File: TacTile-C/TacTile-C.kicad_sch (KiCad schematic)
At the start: 42 parts, among them J1 Conn_01x02, J10 Conn_01x02, J11 Conn_01x02, J12 Conn_01x02, J13 Conn_01x02, J14 Conn_01x02, J15 Conn_01x02, J16 Conn_01x02, J17 Conn_01x02, J2 Conn_01x02, J3 Conn_01x02, J4 Conn_01x02, J5 Conn_01x02, J6 Conn_01x02, J7 Conn_01x02, J8 Conn_01x02, J9 Conn_01x02, U1 74HC4051, U10 74LVC1G18, U2 74HC4051, U3 74HC4051, U4 74HC4051, U5 74HC4051, U7 74LVC1G18, U8 74HC4051, U9 74HC4051

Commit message: Began layout and routing of board C
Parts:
- added J18: Conn_01x04, Connector_PinHeader_1.27mm:PinHeader_1x04_P1.27mm_Vertical, symbol Connector_Generic:Conn_01x04
- added J19: Conn_01x05, Connector_PinHeader_1.27mm:PinHeader_1x05_P1.27mm_Vertical, symbol Connector_Generic:Conn_01x05
- added J20, J21: Conn_01x02, Connector_PinHeader_1.27mm:PinHeader_1x02_P1.27mm_Vertical, symbol Connector_Generic:Conn_01x02
- renumbered J2 to J1, J11 to J10, J12 to J11, J13 to J12, J14 to J13, J15 to J14, J16 to J15, J17 to J16, J1 to J17, J3 to J2, J4 to J3, J5 to J4, J6 to J5, J7 to J6, J8 to J7, J9 to J8, J10 to J9, U7 to U1, U10 to U1, U1 to U2, U2 to U3, U3 to U4, U4 to U5, U5 to U6, U8 to U7, U9 to U8
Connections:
- net GND: now also J20.2 (Pin_2)
- net LEN: now also J21.2 (Pin_2)
- net LS0: now also J18.1 (Pin_1)
- net LS1: now also J18.2 (Pin_2)
- net LS2: now also J18.3 (Pin_3)
- net LS3: now also J18.4 (Pin_4)
- net LS4: now also J19.1 (Pin_1)
- net LS5: now also J19.2 (Pin_2)
- net LS6: now also J19.3 (Pin_3)
- net LS7: now also J19.4 (Pin_4)
- net LS8: now also J19.5 (Pin_5)
- net VCC: now also J21.1 (Pin_1)
- net VIN: now also J20.1 (Pin_1)
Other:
- moved on the sheet: J17

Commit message: Mounted ICs without sockets to save space
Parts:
- U1: footprint Package_DIP:DIP-6_W7.62mm_Socket -> Package_DIP:DIP-6_W7.62mm
- U2, U3, U4, U5, U6, U7, U8: footprint Package_DIP:DIP-16_W7.62mm_Socket -> Package_DIP:DIP-16_W7.62mm
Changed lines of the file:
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@@
       (effects (font (size 1.27 1.27)) (justify left))
     )
-    (property "Footprint" "Package_DIP:DIP-16_W7.62mm_Socket" (at 149.86 105.41 0)
+    (property "Footprint" "Package_DIP:DIP-16_W7.62mm" (at 149.86 105.41 0)
       (effects (font (size 1.27 1.27)) hide)
     )
@@
       (effects (font (size 1.27 1.27)) (justify left))
     )
-    (property "Footprint" "Package_DIP:DIP-16_W7.62mm_Socket" (at 135.89 144.78 0)
+    (property "Footprint" "Package_DIP:DIP-16_W7.62mm" (at 135.89 144.78 0)
       (effects (font (size 1.27 1.27)) hide)
     )
@@
       (effects (font (size 1.27 1.27)) (justify left))
     )
-    (property "Footprint" "Package_DIP:DIP-16_W7.62mm_Socket" (at 151.13 227.33 0)
+    (property "Footprint" "Package_DIP:DIP-16_W7.62mm" (at 151.13 227.33 0)
       (effects (font (size 1.27 1.27)) hide)
     )
@@
       (effects (font (size 1.27 1.27)))
     )
-    (property "Footprint" "Package_DIP:DIP-6_W7.62mm_Socket" (at 133.35 172.72 0)
+    (property "Footprint" "Package_DIP:DIP-6_W7.62mm" (at 133.35 172.72 0)
       (effects (font (size 1.27 1.27)) hide)
     )
@@
       (effects (font (size 1.27 1.27)) (justify left))
     )
-    (property "Footprint" "Package_DIP:DIP-16_W7.62mm_Socket" (at 120.65 105.41 0)
+    (property "Footprint" "Package_DIP:DIP-16_W7.62mm" (at 120.65 105.41 0)
       (effects (font (size 1.27 1.27)) hide)
     )
@@
       (effects (font (size 1.27 1.27)) (justify left))
     )
-    (property "Footprint" "Package_DIP:DIP-16_W7.62mm_Socket" (at 120.65 227.33 0)
+    (property "Footprint" "Package_DIP:DIP-16_W7.62mm" (at 120.65 227.33 0)
       (effects (font (size 1.27 1.27)) hide)
     )
@@
       (effects (font (size 1.27 1.27)) (justify left))
     )
-    (property "Footprint" "Package_DIP:DIP-16_W7.62mm_Socket" (at 91.44 105.41 0)
+    (property "Footprint" "Package_DIP:DIP-16_W7.62mm" (at 91.44 105.41 0)
       (effects (font (size 1.27 1.27)) hide)
     )
@@
       (effects (font (size 1.27 1.27)) (justify left))
     )
-    (property "Footprint" "Package_DIP:DIP-16_W7.62mm_Socket" (at 179.07 105.41 0)
+    (property "Footprint" "Package_DIP:DIP-16_W7.62mm" (at 179.07 105.41 0)
       (effects (font (size 1.27 1.27)) hide)
     )
@@
       (effects (font (size 1.27 1.27)) (justify left))
     )
-    (property "Footprint" "Package_DIP:DIP-6_W7.62mm_Socket" (at 177.8 26.67 0)
-      (effects (font (size 1.27 1.27)) hide)
-    )
+    (property "Footprint" "Package_DIP:DIP-6_W7.62mm" (at 177.8 26.67 0)
+      (effects (font (size 1.27 1.27)) hide)
+    )

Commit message: Enlarged B-C interface to 2.54 pitch connectors
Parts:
- J18: footprint Connector_PinHeader_1.27mm:PinHeader_1x04_P1.27mm_Vertical -> Connector_PinHeader_2.54mm:PinHeader_1x04_P2.54mm_Vertical
- J19: footprint Connector_PinHeader_1.27mm:PinHeader_1x05_P1.27mm_Vertical -> Connector_PinHeader_2.54mm:PinHeader_1x05_P2.54mm_Vertical
- J20, J21: footprint Connector_PinHeader_1.27mm:PinHeader_1x02_P1.27mm_Vertical -> Connector_PinHeader_2.54mm:PinHeader_1x02_P2.54mm_Vertical
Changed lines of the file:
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@@
       (effects (font (size 1.27 1.27)) (justify left))
     )
-    (property "Footprint" "Connector_PinHeader_1.27mm:PinHeader_1x05_P1.27mm_Vertical" (at 27.94 132.08 0)
+    (property "Footprint" "Connector_PinHeader_2.54mm:PinHeader_1x05_P2.54mm_Vertical" (at 27.94 132.08 0)
       (effects (font (size 1.27 1.27)) hide)
     )
@@
       (effects (font (size 1.27 1.27)) (justify left))
     )
-    (property "Footprint" "Connector_PinHeader_1.27mm:PinHeader_1x02_P1.27mm_Vertical" (at 27.94 147.32 0)
+    (property "Footprint" "Connector_PinHeader_2.54mm:PinHeader_1x02_P2.54mm_Vertical" (at 27.94 147.32 0)
       (effects (font (size 1.27 1.27)) hide)
     )
@@
       (effects (font (size 1.27 1.27)) (justify left))
     )
-    (property "Footprint" "Connector_PinHeader_1.27mm:PinHeader_1x02_P1.27mm_Vertical" (at 27.94 162.56 0)
+    (property "Footprint" "Connector_PinHeader_2.54mm:PinHeader_1x02_P2.54mm_Vertical" (at 27.94 162.56 0)
       (effects (font (size 1.27 1.27)) hide)
     )
@@
       (effects (font (size 1.27 1.27)) (justify left))
     )
-    (property "Footprint" "Connector_PinHeader_1.27mm:PinHeader_1x04_P1.27mm_Vertical" (at 27.94 115.57 0)
-      (effects (font (size 1.27 1.27)) hide)
-    )
+    (property "Footprint" "Connector_PinHeader_2.54mm:PinHeader_1x04_P2.54mm_Vertical" (at 27.94 115.57 0)
+      (effects (font (size 1.27 1.27)) hide)
+    )

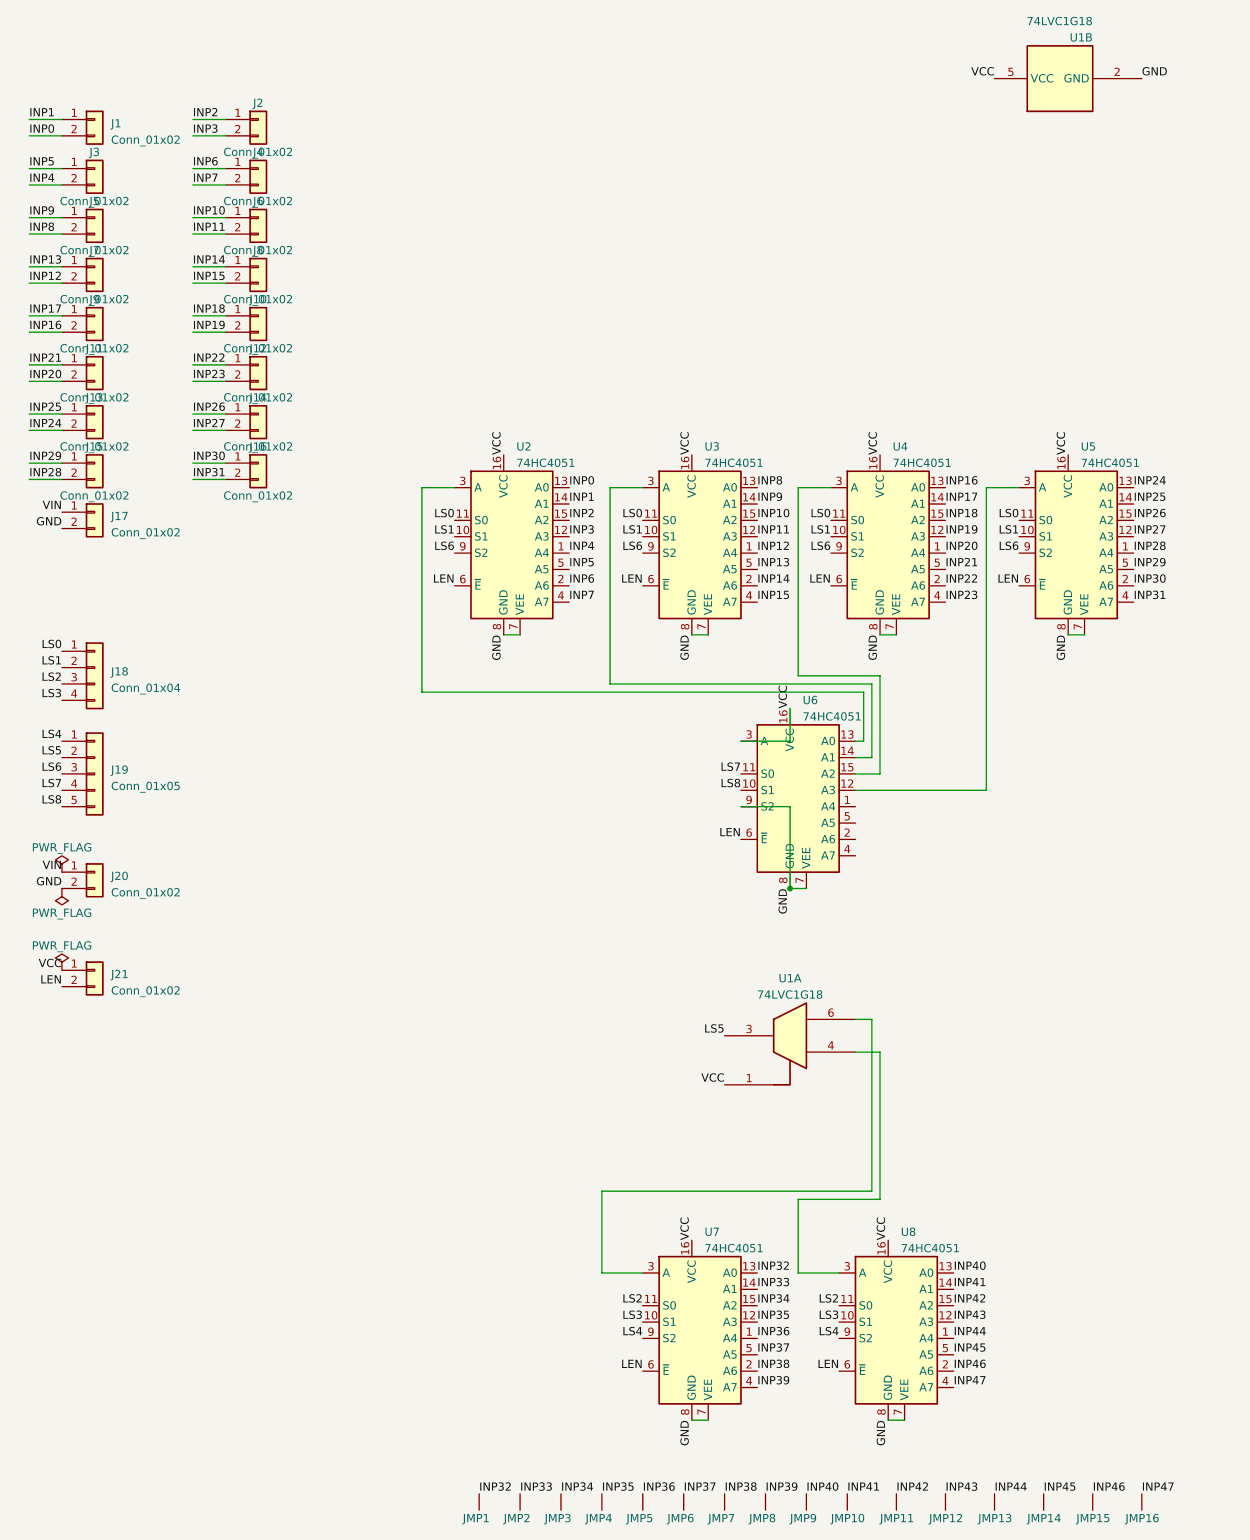
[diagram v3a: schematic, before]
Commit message: Used 16DIP demultiplexer instead of single demultiplexer
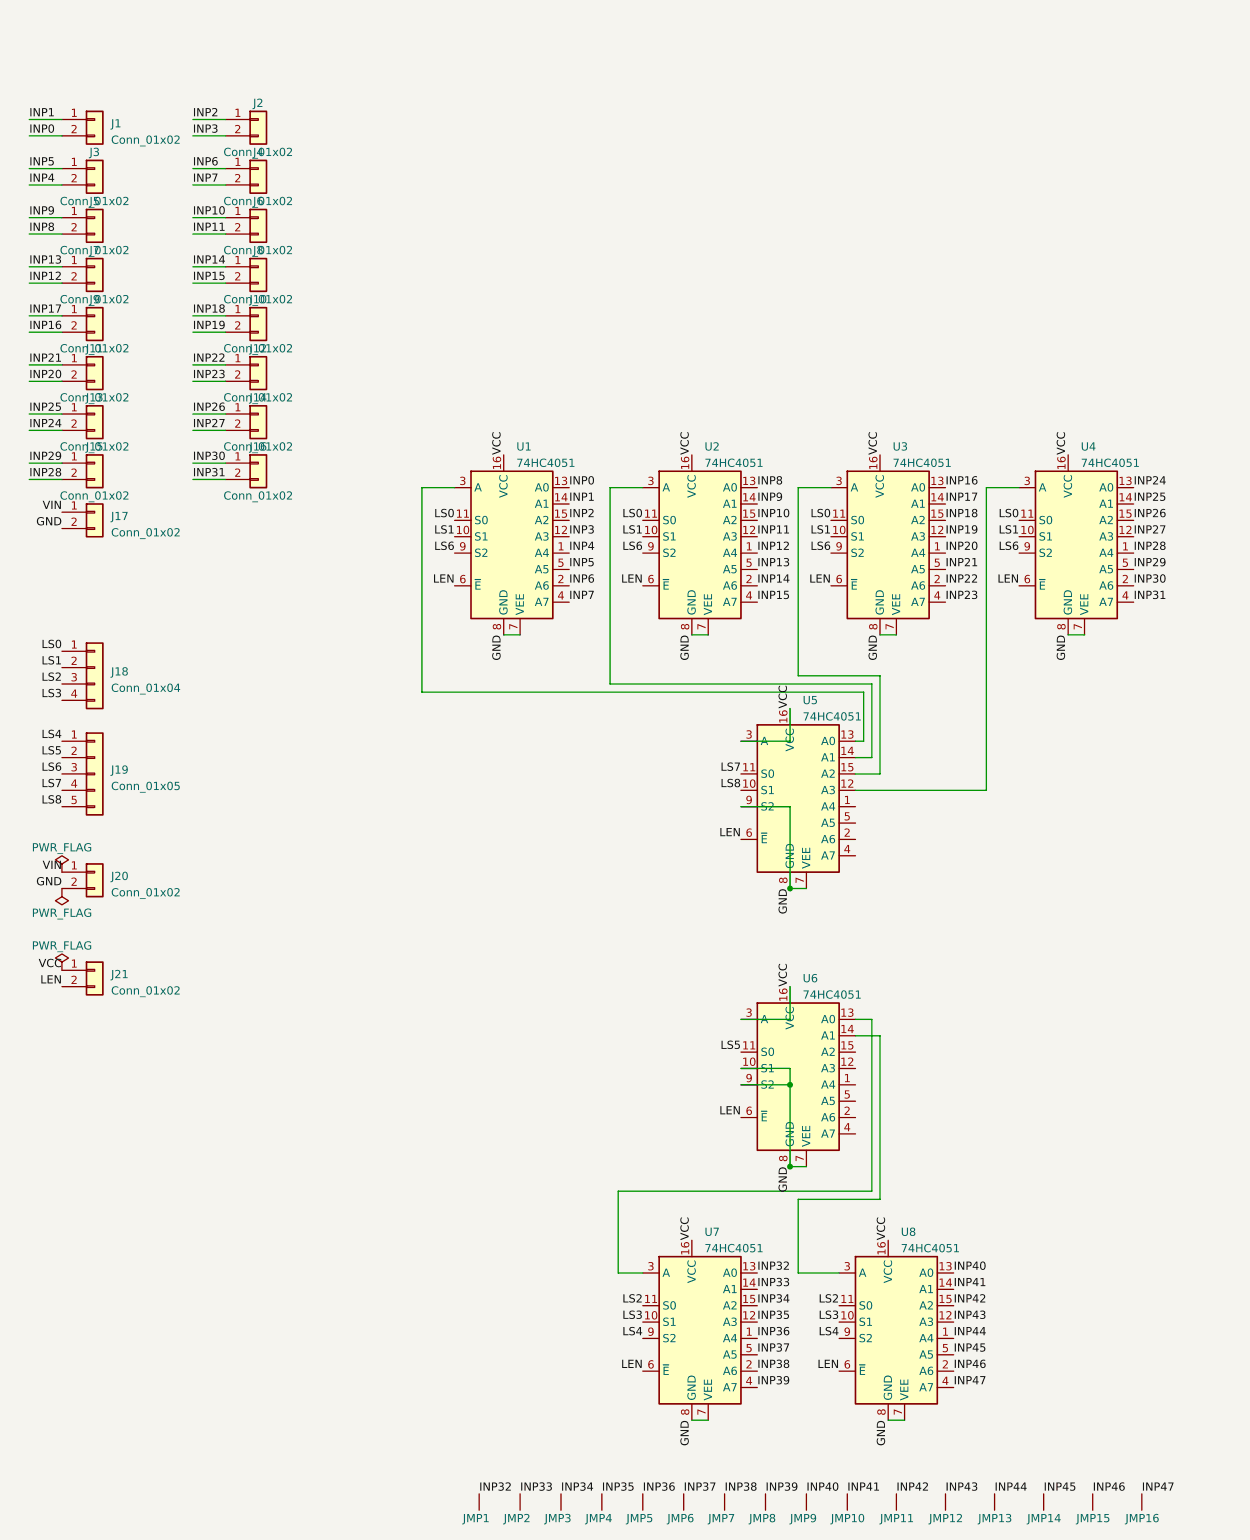
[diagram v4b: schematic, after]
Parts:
- removed U1: 74LVC1G18, Package_DIP:DIP-6_W7.62mm, symbol 74xGxx:74LVC1G18
- added U6: 74HC4051, Package_DIP:DIP-16_W7.62mm, symbol 74xx:74HC4051
- renumbered U2 to U1, U3 to U2, U4 to U3, U5 to U4, U6 to U5
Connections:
- net GND: now also U6.10 (S1), U6.7 (VEE), U6.8 (GND), U6.9 (S2)
- net LEN: now also U6.6 (~{E})
- net LS5: now also U6.11 (S0)
- net VCC: now also U6.16 (VCC), U6.3 (A)
- net at U8.3 (A): now also U6.14 (A1)
- net at U7.3 (A): now also U6.13 (A0)

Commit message: Redid A board with MOSFETs sinking current
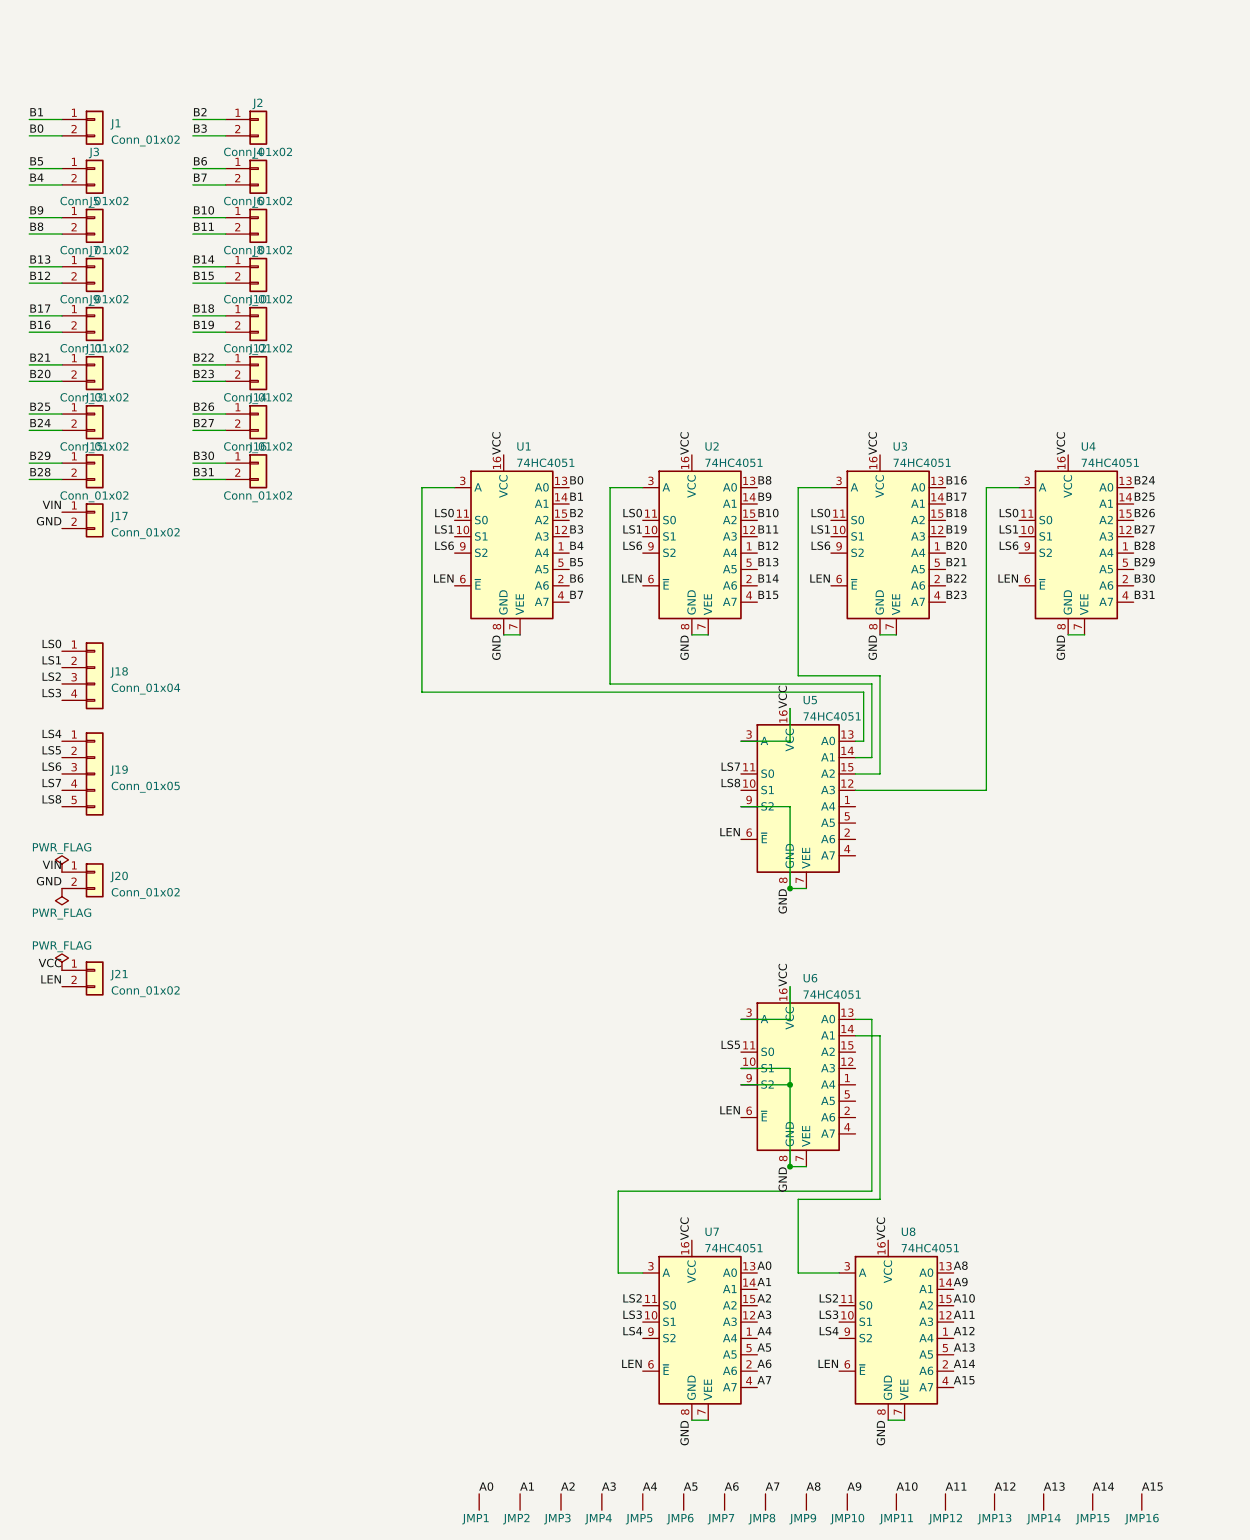
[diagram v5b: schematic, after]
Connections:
- net INP0 renamed B0
- net INP1 renamed B1
- net INP10 renamed B10
- net INP11 renamed B11
- net INP12 renamed B12
- net INP13 renamed B13
- net INP14 renamed B14
- net INP15 renamed B15
- net INP16 renamed B16
- net INP17 renamed B17
- net INP18 renamed B18
- net INP19 renamed B19
- net INP2 renamed B2
- net INP20 renamed B20
- net INP21 renamed B21
- net INP22 renamed B22
- net INP23 renamed B23
- net INP24 renamed B24
- net INP25 renamed B25
- net INP26 renamed B26
- net INP27 renamed B27
- net INP28 renamed B28
- net INP29 renamed B29
- net INP3 renamed B3
- net INP30 renamed B30
- net INP31 renamed B31
- net INP32 renamed A0
- net INP33 renamed A1
- net INP34 renamed A2
- net INP35 renamed A3
- net INP36 renamed A4
- net INP37 renamed A5
- net INP38 renamed A6
- net INP39 renamed A7
- net INP4 renamed B4
- net INP40 renamed A8
- net INP41 renamed A9
- net INP42 renamed A10
- net INP43 renamed A11
- net INP44 renamed A12
- net INP45 renamed A13
- net INP46 renamed A14
- net INP47 renamed A15
- net INP5 renamed B5
- net INP6 renamed B6
- net INP7 renamed B7
- net INP8 renamed B8
- net INP9 renamed B9

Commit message: Added voltage input to A MOSFETs
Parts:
- added JMP17: ~, TacTile:Jumper_Connect, symbol TacTile:Jumper_Connect
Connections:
- net VCC: now also JMP17.1 (A)
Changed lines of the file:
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@@
+    (effects (font (size 1.27 1.27)) (justify left bottom))
+  )
+  (label "VCC" (at 196.85 243.84 0) (fields_autoplaced)
     (effects (font (size 1.27 1.27)) (justify left bottom))
   )
@@
         )
       )
+    )
+  )
+  (symbol (lib_id "TacTile:Jumper_Connect") (at 196.85 243.84 0) (unit 1)
+    (in_bom yes) (on_board yes) (dnp no) (fields_autoplaced)
+    (property "Reference" "JMP17" (at 198.12 247.015 0)
+      (effects (font (size 1.27 1.27)) (justify left))
+    )
+    (property "Value" "~" (at 196.85 243.84 0)
+      (effects (font (size 1.27 1.27)))
+    )
+    (property "Footprint" "TacTile:Jumper_Connect" (at 196.85 243.84 0)
+      (effects (font (size 1.27 1.27)) hide)
+    )
+    (property "Datasheet" "" (at 196.85 243.84 0)
+      (effects (font (size 1.27 1.27)) hide)
+    )
+    (pin "1")
+    (instances
+      (project "TacTile-C"
+        (path "/36638316-989c-497b-a9a8-6f6d869c219d"
+          (reference "JMP17") (unit 1)
+        )
+      )
